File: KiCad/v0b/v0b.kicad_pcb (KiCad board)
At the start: 2 copper layers, 93 x 58.4 mm, 36 parts, among them U1 SST39SF040, U10 MCP1700, U2 74HC139, U3 74HC174, U4 74HC191, U5 74HC191, U6 74HC191, U7 74HC670, U8 62256, U9 SAM2695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

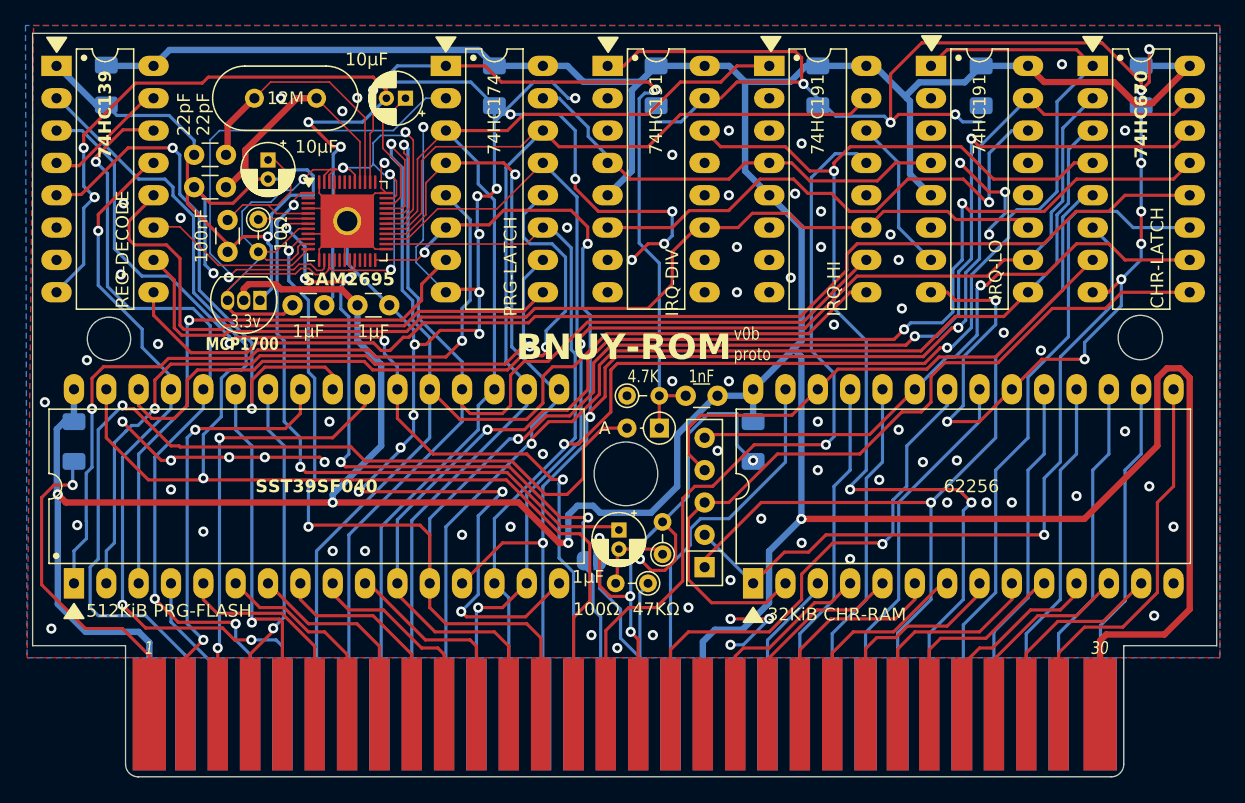
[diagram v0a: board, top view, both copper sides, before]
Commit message: update v0b and README documentation
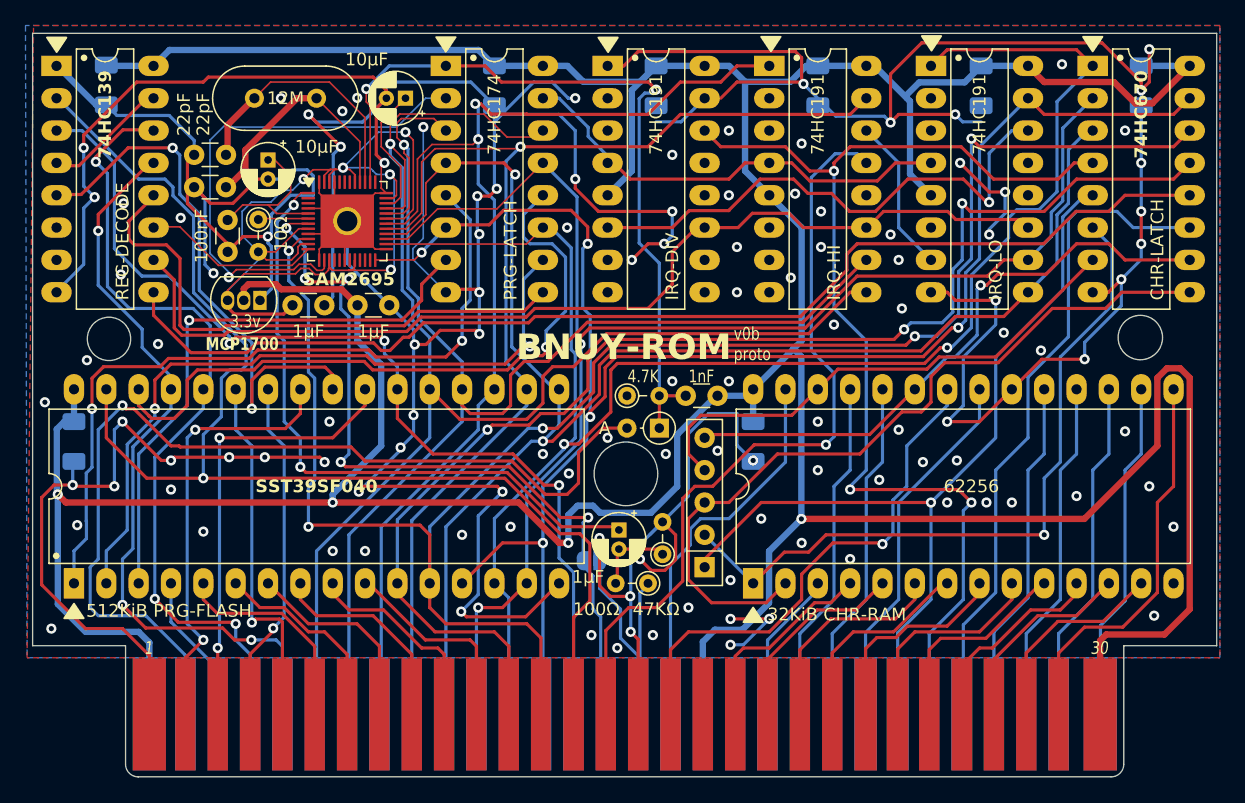
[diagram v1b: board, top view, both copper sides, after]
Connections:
- U3 pad 14: /cD4 -> /cD7
- U3 pad 3: /cD5 -> /cD6
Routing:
- net GND: track 534.8 -> 550.2 mm, vias 117 -> 120
- net /cD7: track 97.3 -> 112.2 mm
- net /cD6: track 97.1 -> 103.1 mm
- net /cD4: track 95.8 -> 93.8 mm, vias 0 -> 1
- net +3V3: track 81.5 -> 82.7 mm
- net /cD5: track 88.8 -> 89.7 mm, vias 0 -> 2
- net /cD3: track 121.7 -> 120.9 mm
- net /~{ROMSEL}: track 76.6 -> 75.9 mm
- net /~{RESET}: track 61.0 -> 61.6 mm

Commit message: update v0b
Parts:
- added JP2: SolderJumper_2_Open, Jumper:SolderJumper-2_P1.3mm_Open_RoundedPad1.0x1.5mm, B.Cu at (115.6, 50.8)
- added JP3: SolderJumper_2_Open, Jumper:SolderJumper-2_P1.3mm_Open_RoundedPad1.0x1.5mm, B.Cu at (115.6, 45.7)
- added JP4: SolderJumper_2_Open, Jumper:SolderJumper-2_P1.3mm_Open_RoundedPad1.0x1.5mm, B.Cu at (115.6, 48.3)
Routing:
- net GND: track 550.2 -> 539.8 mm, vias 120 -> 127
- net /pBank1: track 61.7 -> 70.9 mm
- net /pA11: track 67.8 -> 76.6 mm, vias 1 -> 3
- net /pA12: track 89.1 -> 95.2 mm
- net /pBank2: track 41.1 -> 45.3 mm
- net /cD5: track 89.7 -> 92.1 mm
- net /pA13: track 52.7 -> 54.8 mm, vias 0 -> 1
- net /~{RESET}: track 61.6 -> 62.8 mm
- net /R~{W}: track 98.4 -> 97.4 mm
- net /cBank3: track 59.9 -> 60.5 mm
- net /pBank0: track 47.0 -> 47.6 mm, vias 1 -> 2
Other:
- board text added: "NO670"
